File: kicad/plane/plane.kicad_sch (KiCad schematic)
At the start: 11 parts, among them J1 Raspberry_Pi_4, M1 Left_Aileron_Servo, M2 Right_Aileron_Servo, M3 Elevator_Servo, M4 Rudder_Servo, U1 LD1085V50, U2 LD1085V50, U3 NRF24L01_Breakout, U4 AMS1117, X1 ESC 5V/2A

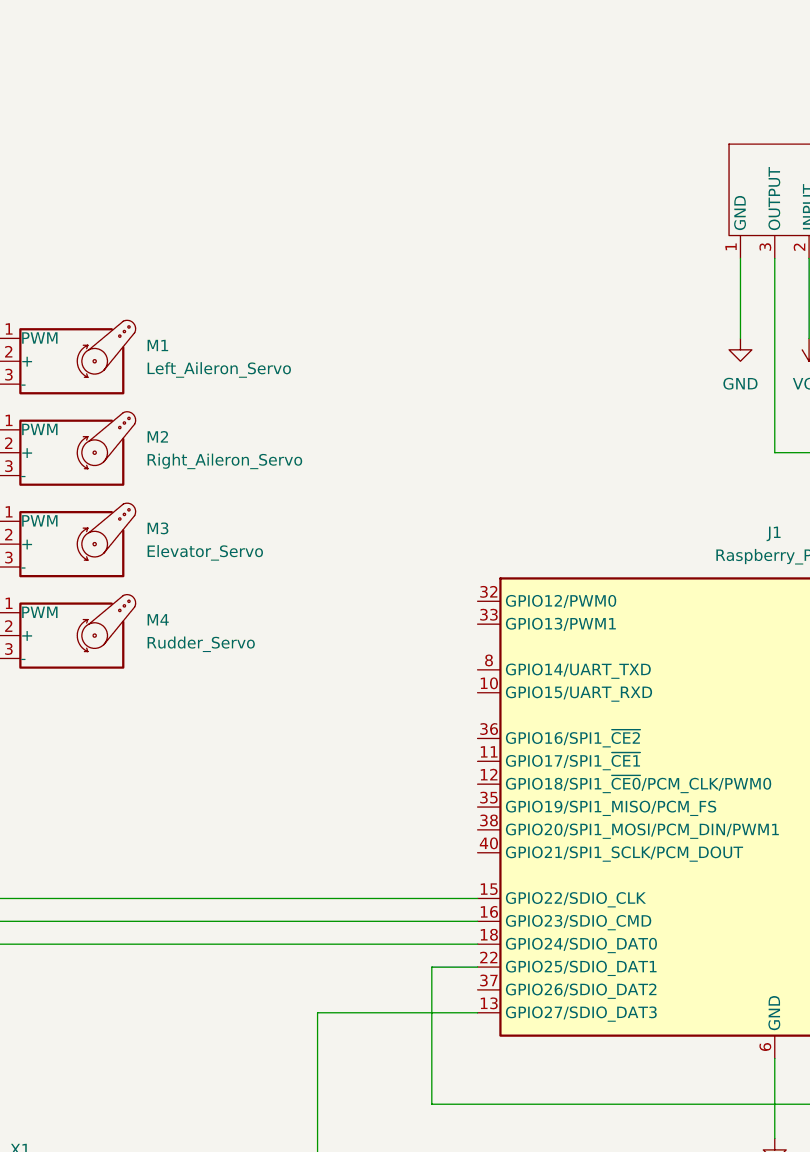
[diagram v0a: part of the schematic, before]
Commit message: i forgot leds in kicad schematic... ops
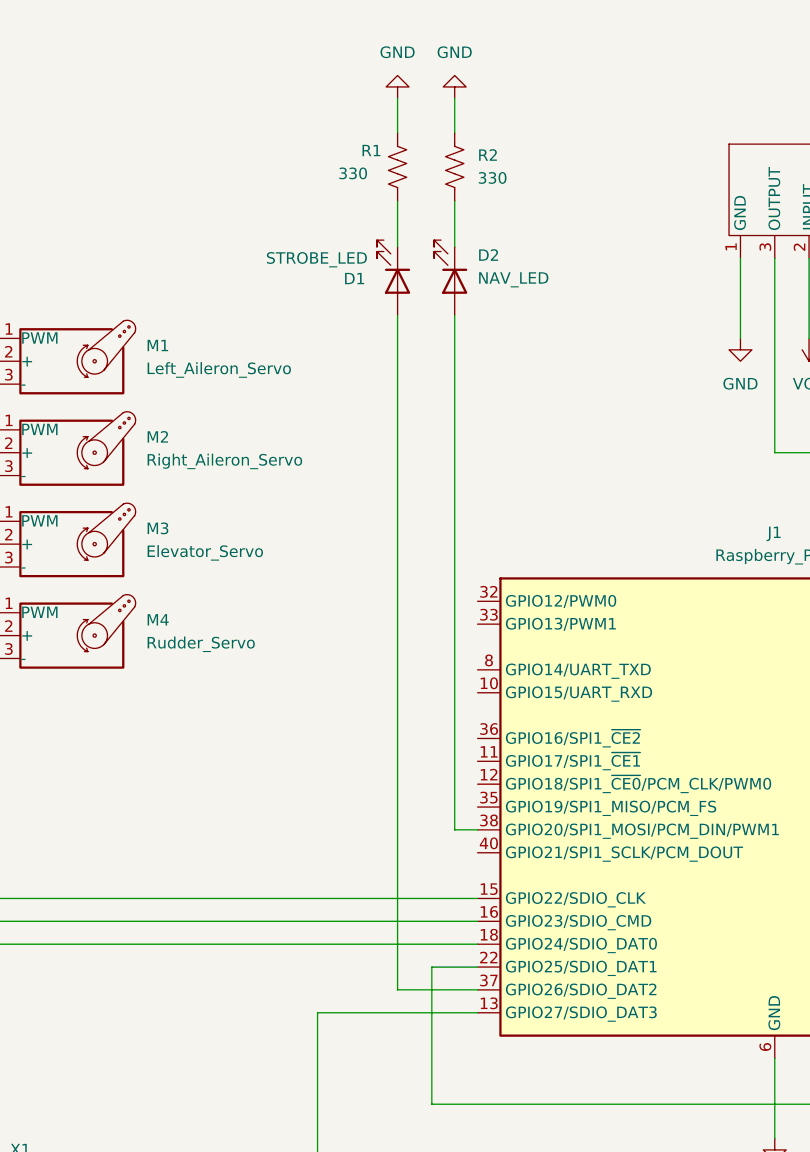
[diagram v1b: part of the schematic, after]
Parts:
- added D1: STROBE_LED, symbol Device:LED
- added D2: NAV_LED, symbol Device:LED
- added R1, R2: 330, symbol Device:R_US
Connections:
- net GND: now also R1.1, R2.1
- net at J1.37 (GPIO26/SDIO_DAT2): now also D1.2 (A)
- net at J1.38 (GPIO20/SPI1_MOSI/PCM_DIN/PWM1): now also D2.2 (A)
- new net: D1.1 (K), R1.2
- new net: D2.1 (K), R2.2

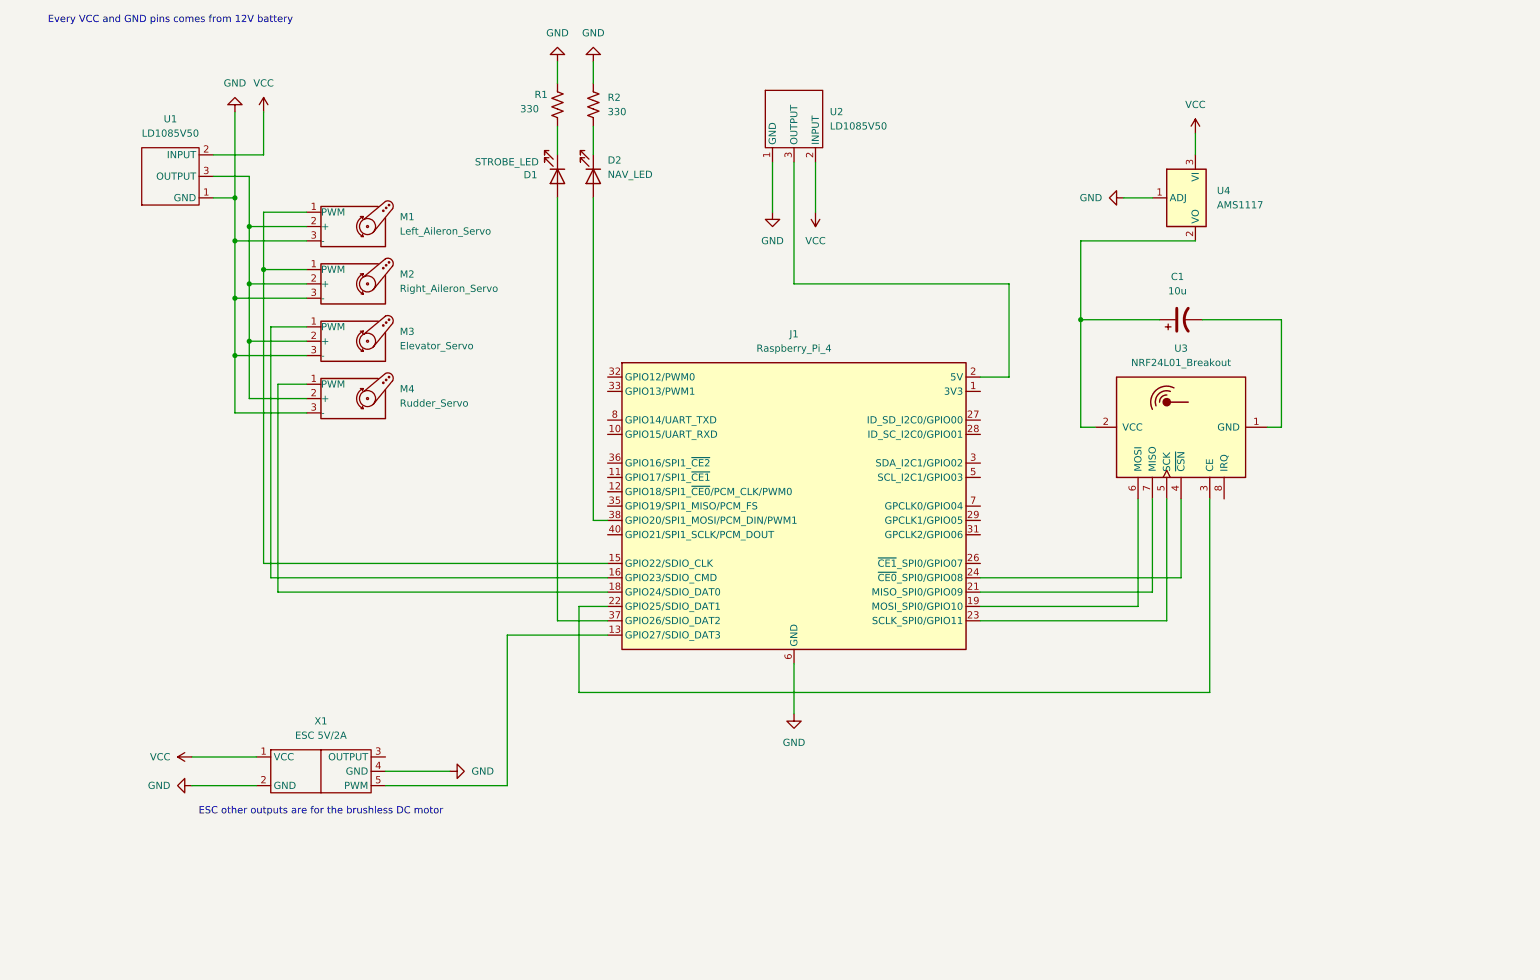
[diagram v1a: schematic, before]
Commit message: kicad plane project, added first plane code structure
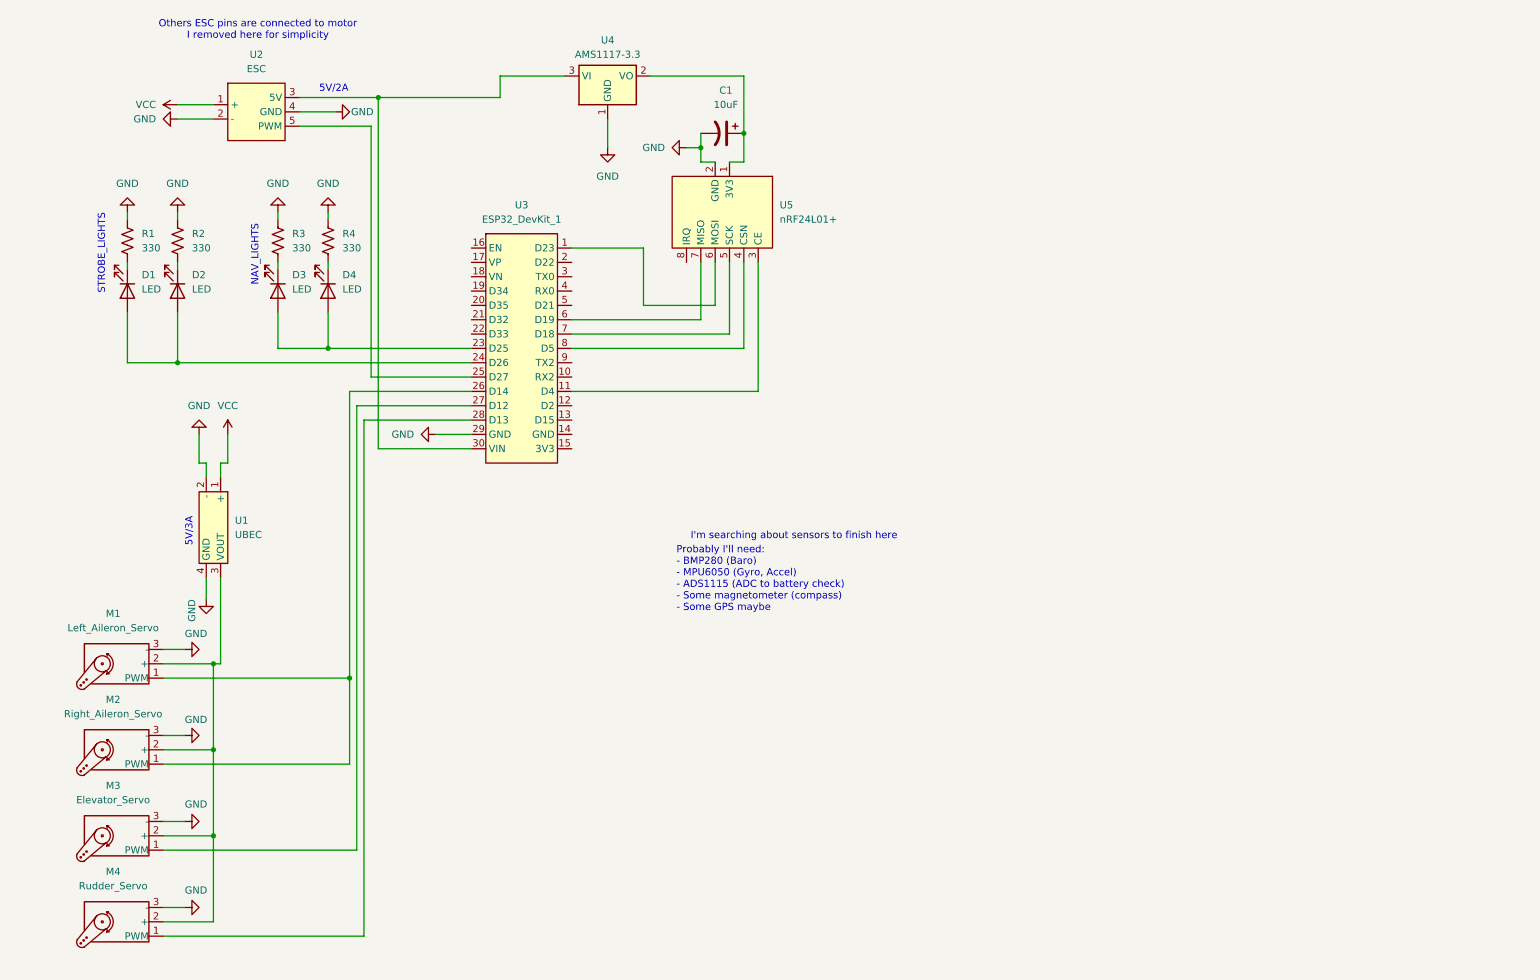
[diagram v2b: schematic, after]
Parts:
- removed J1: Raspberry_Pi_4, symbol Connector:Raspberry_Pi_4
- removed U1, U2: LD1085V50, LD1085V50:TO220, symbol RCAirplane_components:LD1085V50
- removed U3: NRF24L01_Breakout, RF_Module:nRF24L01_Breakout, symbol RF:NRF24L01_Breakout
- removed U4: AMS1117, Package_TO_SOT_SMD:SOT-223-3_TabPin2, symbol Regulator_Linear:AMS1117
- removed X1: ESC 5V/2A, symbol RCAirplane_components:ESC
- added D3, D4: LED, symbol Device:LED
- added R3, R4: 330, symbol Device:R_US
- added U1: UBEC, symbol PlaneComponents:Buck_Converter
- added U2: ESC, symbol PlaneComponents:ESC
- added U3: ESP32_DevKit_1, symbol PlaneComponents:ESP32_DevKit_1
- added U4: AMS1117-3.3, Package_TO_SOT_SMD:SOT-223-3_TabPin2, symbol Regulator_Linear:AMS1117-3.3
- added U5: nRF24L01+, symbol PlaneComponents:nRF24L01+
- C1: value 10u -> 10uF
- D1: value STROBE_LED -> LED
- D2: value NAV_LED -> LED
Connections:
- net GND: now also C1.2, R3.1, R4.1, U1.2 (-), U1.4 (GND), U2.2 (-), U2.4 (GND), U3.29 (GND), U4.1 (GND), U5.2 (GND)
- net VCC: now also U1.1 (+), U2.1 (+)
- net at C1.1: now also U4.2 (VO), U5.1 (3V3)
- net at M1.2 (+), M2.2 (+), M3.2 (+)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: now also U1.3 (VOUT)
- net at D1.2 (A): now also D2.2 (A), U3.24 (D26)
- net at M1.1 (PWM), M2.1 (PWM): now also U3.26 (D14)
- net at M3.1 (PWM): now also U3.27 (D12)
- net at M4.1 (PWM): now also U3.28 (D13)
- new net: D3.1 (K), R3.2
- new net: D3.2 (A), D4.2 (A), U3.23 (D25)
- new net: U3.1 (D23), U5.6 (MOSI)
- new net: U3.11 (D4), U5.3 (CE)
- new net: U2.5 (PWM), U3.25 (D27)
- new net: U2.3 (5V), U3.30 (VIN), U4.3 (VI)
- new net: U3.6 (D19), U5.7 (MISO)
- new net: U3.7 (D18), U5.5 (SCK)
- new net: U3.8 (D5), U5.4 (CSN)
- new net: D4.1 (K), R4.2
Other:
- note added: "5V/2A"
- note added: "5V/3A"
- note added: "I'm searching about sensors to finish here"
- note added: "NAV_LIGHTS"
- note added: "Others ESC pins are connected to motor I removed here for simplicity"
- note added: "Probably I'll need: - BMP280 (Baro) - MPU6050 (Gyro, Accel) - ADS1115 (ADC to battery check) - Some magnetometer (compass) - Some GPS maybe"
- note added: "STROBE_LIGHTS"
- note removed: "ESC other outputs are for the brushless DC motor"
- note removed: "Every VCC and GND pins comes from 12V battery"
- company: Breno Soares Alves -> Breno S. Alves

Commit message: plane schematic finished
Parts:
- removed U1: UBEC, symbol PlaneComponents:Buck_Converter
- added J1: Battery, Connector_Phoenix_MSTB:PhoenixContact_MSTBV_2,5_2-GF_1x02_P5.00mm_Vertical_ThreadedFlange, symbol Connector_Generic:Conn_01x02
- added U1, U3: LD1085V50, symbol PlaneComponents:LD1085V50
- added U10: GY - GPS6MV2, symbol PlaneComponents:GY_-_GPS6MV2
- added U6: GY - BMP280, Package_LGA:Bosch_LGA-8_2x2.5mm_P0.65mm_ClockwisePinNumbering, symbol PlaneComponents:GY - BMP280
- added U8: GY-521 - MPU6050, symbol PlaneComponents:GY-521 - MPU6050
- added U9: GY273 - HMC5883L, symbol PlaneComponents:GY273 - HMC5883L
- renumbered U3 to U4, U4 to U5, U5 to U7
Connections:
- net GND: now also J1.1 (Pin_1), U1.3 (GND), U3.3 (GND)
- net at U4.10 (RX2): now also U10.4 (TX)
- net at U4.14 (GND): now also U10.2 (GND), U6.2 (GND), U6.6 (SDO/MISO), U8.2 (GND), U8.7 (AD0), U9.2 (GND)
- net at U4.15 (3V3): now also U10.1 (VCC), U6.1 (VCC), U6.5 (CSB/CS), U8.1 (VCC), U9.1 (VCC)
- net at U4.2 (D22): now also U6.3 (SCL/SCK), U8.3 (SCL), U9.3 (SCL)
- net at U4.5 (D21): now also U6.4 (SDA/MOSI), U8.4 (SDA), U9.4 (SDA)
- net at U4.9 (TX2): now also U10.3 (RX)
- net at M3.2 (+), M4.2 (+): now also U3.2 (VOUT); no longer M1.2 (+), M2.2 (+)
- net VCC: no longer names the net of U2.1 (+)
- net VCC: now also J1.2 (Pin_2), U1.1 (VIN), U3.1 (VIN)
- new net: M1.2 (+), M2.2 (+), U1.2 (VOUT)
- no-connect marks 0 -> 16
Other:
- note added: "Baro"
- note added: "GPS"
- note added: "Gyro/Accel"
- note added: "Magnetometer"
- note removed: "5V/3A"
- note removed: "I'm searching about sensors to finish here"
- note removed: "Probably I'll need: - BMP280 (Baro) - MPU6050 (Gyro, Accel) - ADS1115 (ADC to battery check) - Some magnetometer (compass) - Some GPS maybe"
- moved on the sheet: C1, D1, D2, D3, D4, M1, M2, M3, M4, R1, R2, R3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

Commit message: first footprintsgit add .
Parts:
- added U11: ADS1115, PlaneFootprints:ADS1115, symbol PlaneComponents:ADS1115
- R1, R2, R3, R4, U8: footprint (none) -> Resistor_THT:R_Axial_DIN0207_L6.3mm_D2.5mm_P7.62mm_Horizontal
- U1, U3: footprint (none) -> PlaneFootprints:LD1085V50
- U4: footprint (none) -> PlaneFootprints:ESP32_DevKit_C
- U7: footprint (none) -> PlaneFootprints:nRF24L01+
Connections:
- net GND: now also U11.2 (GND), U11.5 (ADDR)
- net at U4.2 (D22), U6.3 (SCL/SCK), U8.3 (SCL)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: now also U11.3 (SCL)
- net at U2.3 (5V), U4.30 (VIN), U5.3 (VI): now also U11.1 (VDD)
- net at U4.5 (D21), U6.4 (SDA/MOSI), U8.4 (SDA)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: now also U11.4 (SDA)
- no-connect marks 16 -> 20
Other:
- note added: "I need to study about voltage divider to be capable to input battery voltage in conversor to measure battery"

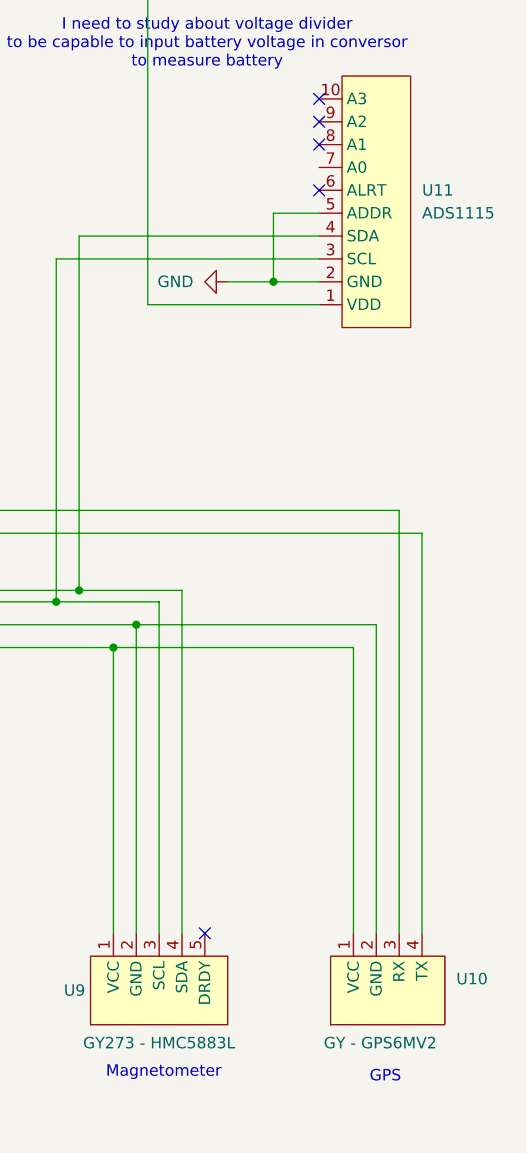
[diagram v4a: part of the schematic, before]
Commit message: footprints finished (still need make T Deans connector to battery and ESC), pcb started (size IS A REAL PROBLEM)
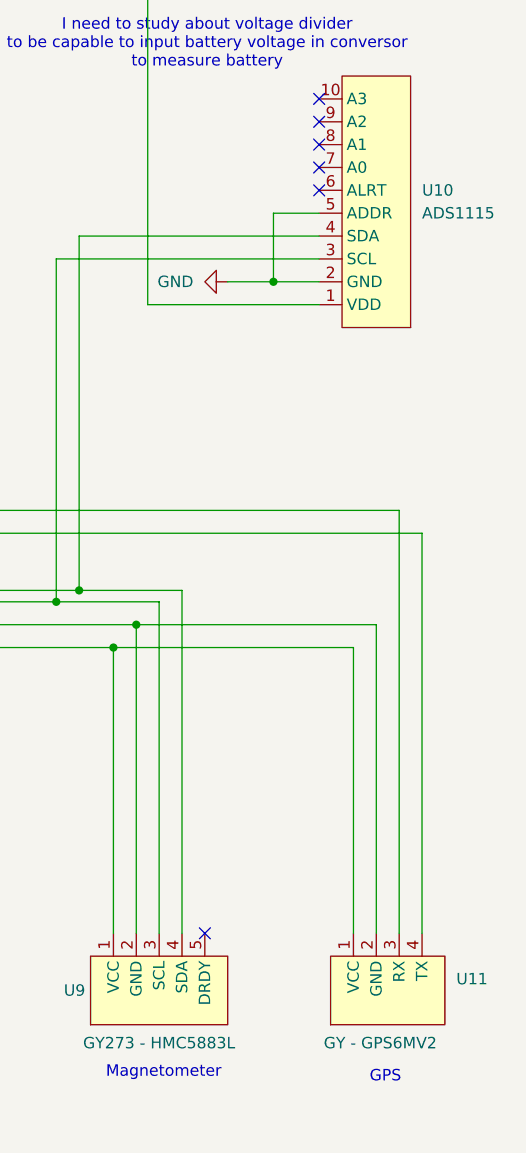
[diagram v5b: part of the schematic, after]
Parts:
- C1: footprint (none) -> Capacitor_THT:CP_Radial_D8.0mm_P2.50mm
- D1, D2, D3, D4: footprint (none) -> PlaneFootprints:LED
- J1: footprint Connector_Phoenix_MSTB:PhoenixContact_MSTBV_2,5_2-GF_1x02_P5.00mm_Vertical_ThreadedFlange -> (none)
- M1, M2, M3, M4: footprint (none) -> Connector_PinHeader_2.54mm:PinHeader_1x03_P2.54mm_Vertical
- U11: renamed from U10; footprint (none) -> PlaneFootprints:GPS6MV2
- U6: footprint Package_LGA:Bosch_LGA-8_2x2.5mm_P0.65mm_ClockwisePinNumbering -> PlaneFootprints:BMP280
- U8: footprint Resistor_THT:R_Axial_DIN0207_L6.3mm_D2.5mm_P7.62mm_Horizontal -> PlaneFootprints:MPU6050
- U9: footprint (none) -> PlaneFootprints:HMC5883L
- renumbered U11 to U10
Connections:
- no-connect marks 20 -> 21
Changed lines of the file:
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@@
 	)
 	(no_connect
+		(at 257.81 41.91)
+	)
+	(no_connect
 		(at 162.56 64.77)
 	)
@@
 			)
 		)
-		(property "Footprint" ""
+		(property "Footprint" "PlaneFootprints:LED"
 			(at 110.49 67.31 0)
 			(effects
@@
 	)
 	(symbol
+		(lib_name "LD1085V50_1")
 		(lib_id "PlaneComponents:LD1085V50")
 		(at 111.76 109.22 180)
@@
 			)
 		)
-		(property "Footprint" ""
+		(property "Footprint" "PlaneFootprints:LED"
 			(at 119.38 67.31 0)
 			(effects
@@
 			)
 		)
-		(property "Footprint" ""
+		(property "Footprint" "PlaneFootprints:LED"
 			(at 83.82 67.31 0)
 			(effects
@@
 			)
 		)
-		(property "Footprint" ""
+		(property "Footprint" "Connector_PinHeader_2.54mm:PinHeader_1x03_P2.54mm_Vertical"
 			(at 82.55 143.764 0)
 			(effects
@@
 			)
 		)
-		(property "Footprint" ""
+		(property "Footprint" "Connector_PinHeader_2.54mm:PinHeader_1x03_P2.54mm_Vertical"
 			(at 82.55 128.524 0)
 			(effects
@@
 			)
 		)
-		(property "Footprint" "Resistor_THT:R_Axial_DIN0207_L6.3mm_D2.5mm_P7.62mm_Horizontal"
+		(property "Footprint" "PlaneFootprints:MPU6050"
 			(at 210.82 133.35 0)
 			(effects
@@
 			)
 		)
-		(property "Footprint" ""
+		(property "Footprint" "PlaneFootprints:HMC5883L"
 			(at 240.03 133.35 0)
 			(effects
@@
 			)
 		)
-		(property "Footprint" ""
+		(property "Footprint" "Capacitor_THT:CP_Radial_D8.0mm_P2.50mm"
 			(at 189.23 39.37 0)
 			(effects
@@
 		(dnp no)
 		(fields_autoplaced yes)
-		(property "Reference" "U11"
+		(property "Reference" "U10"
 			(at 269.24 44.4499 0)
 			(effects
@@
 			(project ""
 				(path "/8dfaeffa-e22f-4849-a554-6a54b7fa5ece"
-					(reference "U11")
+					(reference "U10")
 					(unit 1)
 				)
@@
 			)
 		)
-		(property "Footprint" "Connector_Phoenix_MSTB:PhoenixContact_MSTBV_2,5_2-GF_1x02_P5.00mm_Vertical_ThreadedFlange"
+		(property "Footprint" ""
 			(at 43.18 36.83 0)
 			(effects
@@
 		(on_board yes)
 		(dnp no)
-		(property "Reference" "U10"
+		(property "Reference" "U11"
 			(at 273.05 132.0799 90)
 			(effects
@@
 			)
 		)
-		(property "Footprint" ""
+		(property "Footprint" "PlaneFootprints:GPS6MV2"
 			(at 265.43 133.35 0)
 			(effects
@@
 			(project ""
 				(path "/8dfaeffa-e22f-4849-a554-6a54b7fa5ece"
-					(reference "U10")
+					(reference "U11")
 					(unit 1)
 				)
@@
 			)
 		)
-		(property "Footprint" ""
+		(property "Footprint" "Connector_PinHeader_2.54mm:PinHeader_1x03_P2.54mm_Vertical"
 			(at 82.55 159.004 0)
 			(effects
@@
 			)
 		)
-		(property "Footprint" ""
+		(property "Footprint" "PlaneFootprints:LED"
 			(at 92.71 67.31 0)
 			(effects
@@
 			)
 		)
-		(property "Footprint" "Package_LGA:Bosch_LGA-8_2x2.5mm_P0.65mm_ClockwisePinNumbering"
+		(property "Footprint" "PlaneFootprints:BMP280"
 			(at 181.61 135.89 0)
 			(effects
@@
 			)
 		)
-		(property "Footprint" ""
+		(property "Footprint" "Connector_PinHeader_2.54mm:PinHeader_1x03_P2.54mm_Vertical"
 			(at 82.55 174.244 0)
 			(effects

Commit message: pcb components placement
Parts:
- J1: footprint (none) -> PlaneFootprints:14AWG_Wire
- U2: footprint (none) -> PlaneFootprints:ESC
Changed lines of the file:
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@@
 			)
 		)
-		(property "Footprint" ""
+		(property "Footprint" "PlaneFootprints:14AWG_Wire"
 			(at 43.18 36.83 0)
 			(effects
@@
 			)
 		)
-		(property "Footprint" ""
+		(property "Footprint" "PlaneFootprints:ESC"
 			(at 106.68 35.56 0)
 			(effects
